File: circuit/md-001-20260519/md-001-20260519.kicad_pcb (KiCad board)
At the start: 4 copper layers, 71.4 x 21.3 mm, 41 parts, among them J1 VIN-motor, J2 Conn_Ball_Catch, J3 Conn_relay

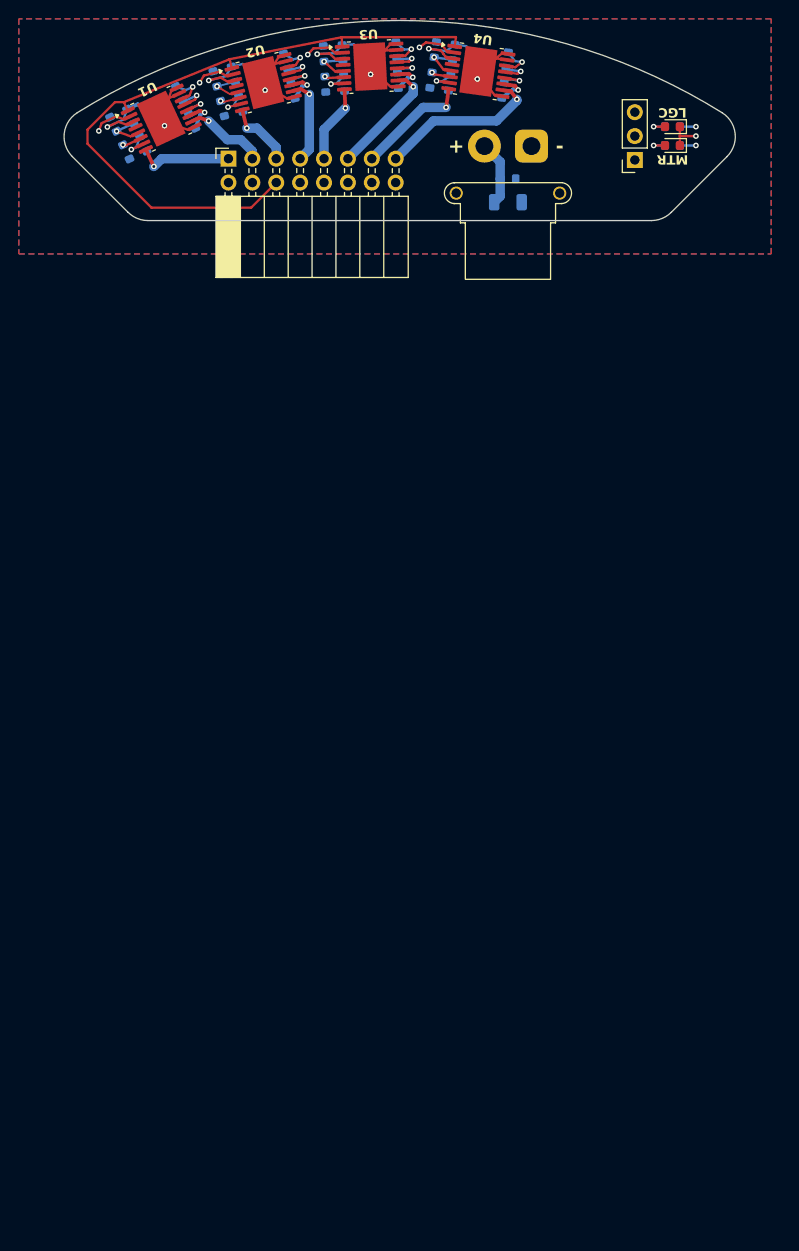
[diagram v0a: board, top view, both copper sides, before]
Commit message: Update MD基板のSMD部品のサイズ変更を完了した
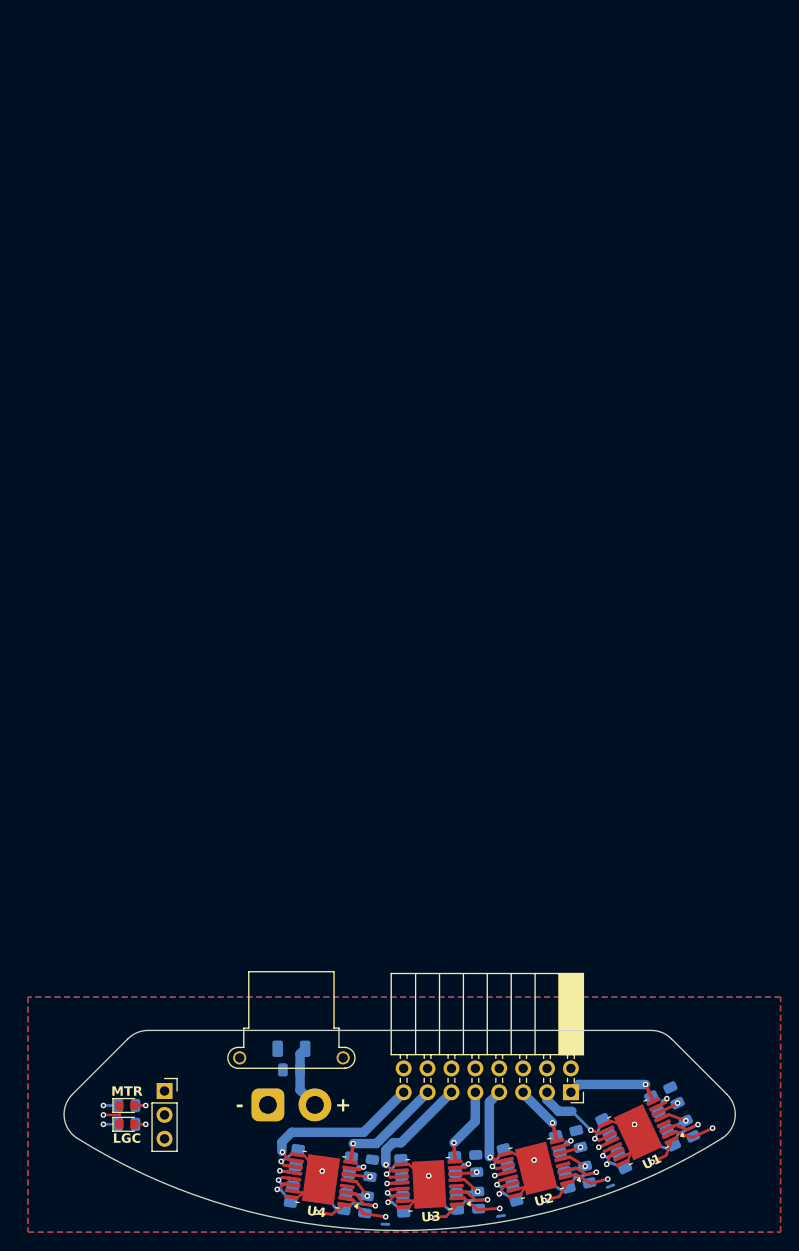
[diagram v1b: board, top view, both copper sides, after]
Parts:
- C1, C10, C11, C12, C13, C2, C3, C4, C5, C6, C7, C8, C9, R1, R10, R11, R12, R13, R14, R15, R16, R17, R18, R2, R3, R4, R5, R6, R7, R8, R9: footprint Resistor_SMD:R_0603_1608Metric -> Resistor_SMD:R_0805_2012Metric
- moved R3 123.1 mm to (30.8, 53.0), turned to -65 degrees
- moved R5 123.0 mm to (19.9, 57.9), turned to -76 degrees
- moved R13 123.0 mm to (-3.58, 61.1), turned to -98 degrees
- moved R11 123.0 mm to (8.34, 60.6), turned to -87 degrees
- moved R1 122.8 mm to (28.8, 53.9), turned to 115 degrees
- moved C1 122.8 mm to (23.6, 56.4), turned to 115 degrees
- moved R2 122.8 mm to (17.8, 58.4), turned to 104 degrees
- moved R10 122.7 mm to (-5.80, 60.7), turned to 82 degrees
- moved C6 122.7 mm to (-11.5, 59.9), turned to 82 degrees
- moved C2 122.7 mm to (12.2, 59.8), turned to 104 degrees
- moved R9 122.7 mm to (6.10, 60.7), turned to 93 degrees
- moved C5 122.7 mm to (0.38, 61.0), turned to 93 degrees
- moved D2 120.9 mm to (-29.0, 52.5), turned to 0 degrees
- moved R18 120.9 mm to (-29.0, 52.5), turned to 0 degrees
- moved C9 119.1 mm to (25.4, 53.4), turned to 115 degrees
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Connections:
- net BALL_CATCH renamed BallCatch_{Back}
- net EN renamed Motor_{EN}
- net OUT1-1 renamed Motor_{OUT1-1}
- net OUT1-2 renamed Motor_{OUT2-1}
- net OUT1-3 renamed Motor_{OUT3-1}
- net OUT1-4 renamed Motor_{OUT4-1}
- net OUT2-1 renamed Motor_{OUT1-2}
- net OUT2-2 renamed Motor_{OUT2-2}
- net OUT2-3 renamed Motor_{OUT3-2}
- net OUT2-4 renamed Motor_{OUT4-2}
- net PH-1 renamed Motor1_{PWM}
- net PH-2 renamed Motor2_{PWM}
- net PH-3 renamed Motor3_{PWM}
- net PH-4 renamed Motor4_{PWM}
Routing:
- net Motor_{EN}: track 71.0 -> 65.4 mm, vias 0 -> 4
- net +3.3V: track 39.9 -> 45.3 mm
- net Motor3_{PWM}: track 19.2 -> 24.1 mm
- net Motor4_{PWM}: track 25.0 -> 22.7 mm
- net GND: track 48.8 -> 51.0 mm
- net Motor_{OUT2-2}: track 9.15 -> 11.1 mm
- net Motor1_{PWM}: track 29.7 -> 31.4 mm
- net Motor_{OUT2-1}: track 7.18 -> 6.55 mm
- net VREF-3: track 4.47 -> 5.06 mm
- net VREF-1: track 4.47 -> 5.06 mm
- net VREF-2: track 4.47 -> 5.06 mm
- net VREF-4: track 4.48 -> 5.06 mm
- net Motor2_{PWM}: track 24.2 -> 24.7 mm
- net Motor_{OUT4-2}: track 17.5 -> 18.0 mm
- net VCC: track 23.9 -> 24.4 mm
- added copper zone on In1.Cu, net GND
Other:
- outline, holes or cut-outs redrawn
- board text added: "R8"

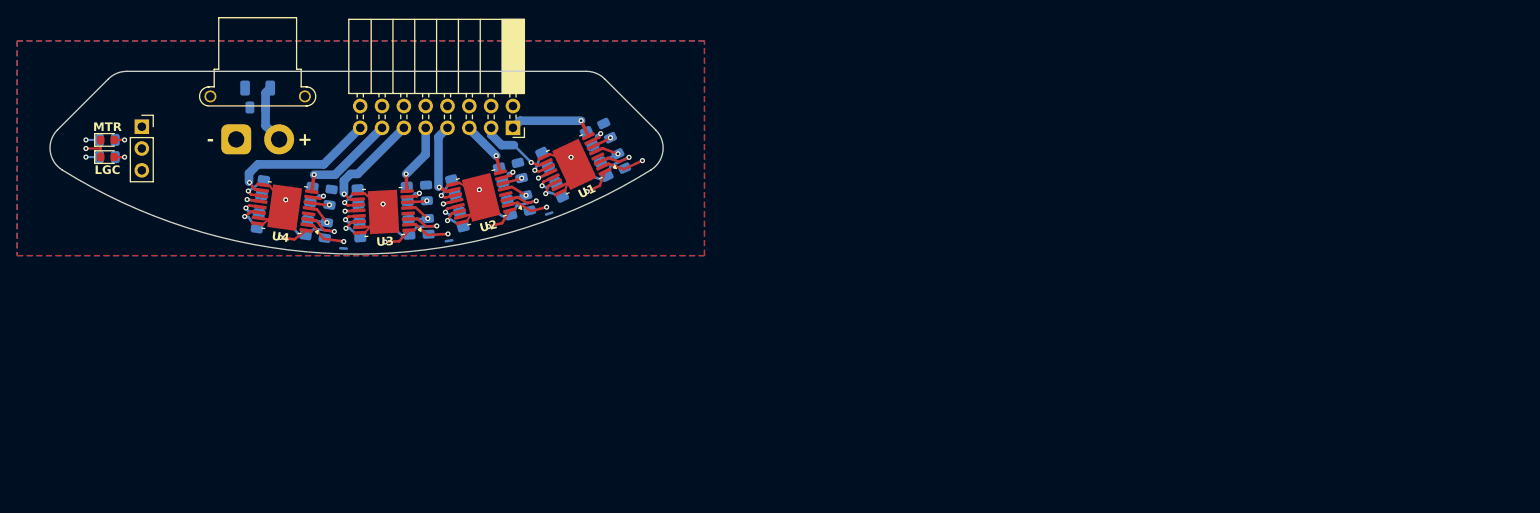
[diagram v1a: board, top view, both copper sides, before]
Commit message: Update MD基板の発注ファイルを更新
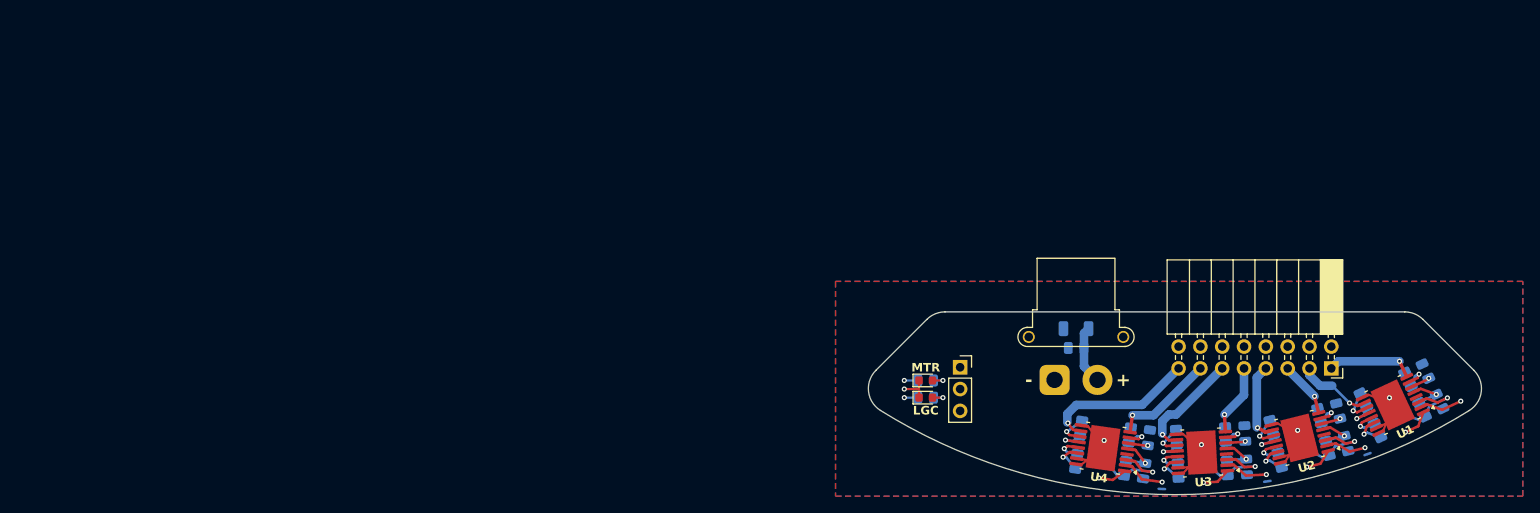
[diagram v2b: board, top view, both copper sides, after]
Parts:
- moved C2 99.3 mm to (107.5, 87.8)
- moved C5 99.3 mm to (95.6, 89.0)
- moved D1 99.3 mm to (66.3, 78.5)
- moved D2 99.3 mm to (66.3, 80.5)
- moved J3 99.3 mm to (113.5, 77.1)
- moved R1 99.3 mm to (124.0, 81.9)
- moved R10 99.3 mm to (89.5, 88.7)
- moved R11 99.3 mm to (103.6, 88.6)
- moved R12 99.3 mm to (101.1, 84.8)
- moved R16 99.3 mm to (92.2, 85.2)
- moved R17 99.3 mm to (66.3, 78.5)
- moved R18 99.3 mm to (66.3, 80.5)
- moved R3 99.3 mm to (126.1, 81.0)
- moved R7 99.3 mm to (124.4, 77.5)
- moved R8 99.3 mm to (114.3, 82.1)
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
